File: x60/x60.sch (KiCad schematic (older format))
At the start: 150 parts, among them SW1 SW_Push, U1 ATmega32U4-AU, Y1 16mhz

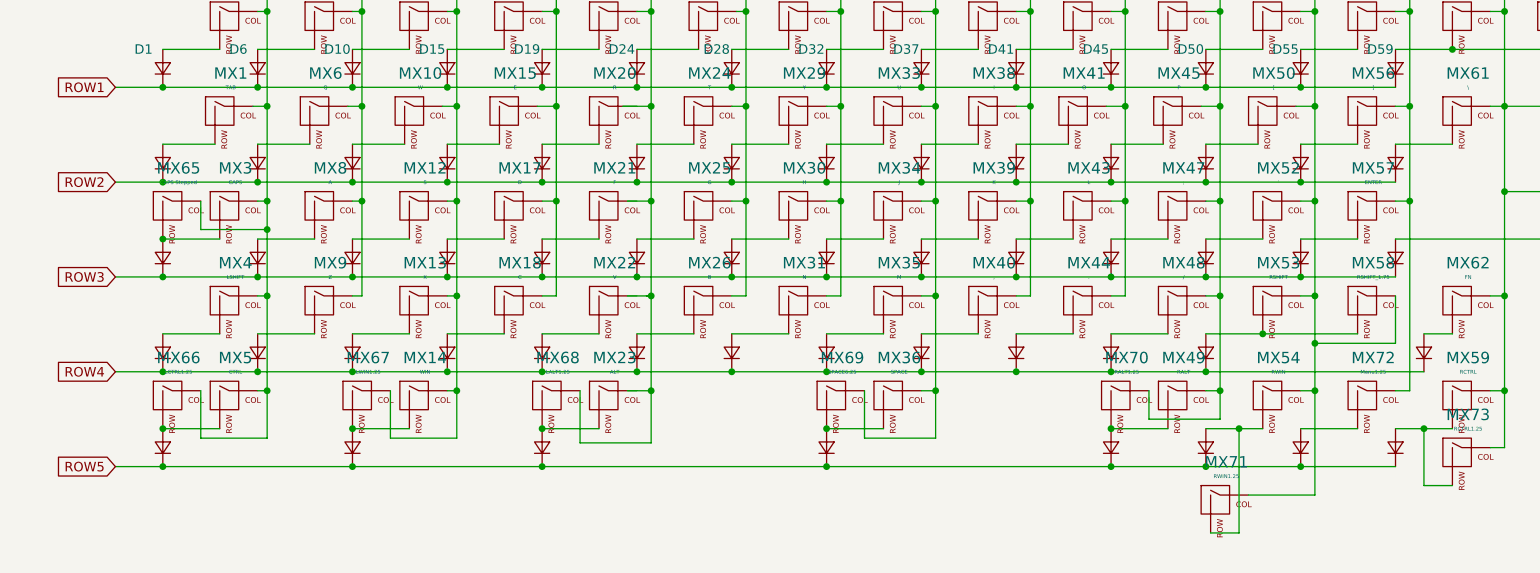
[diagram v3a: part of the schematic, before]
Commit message: aligned diodes
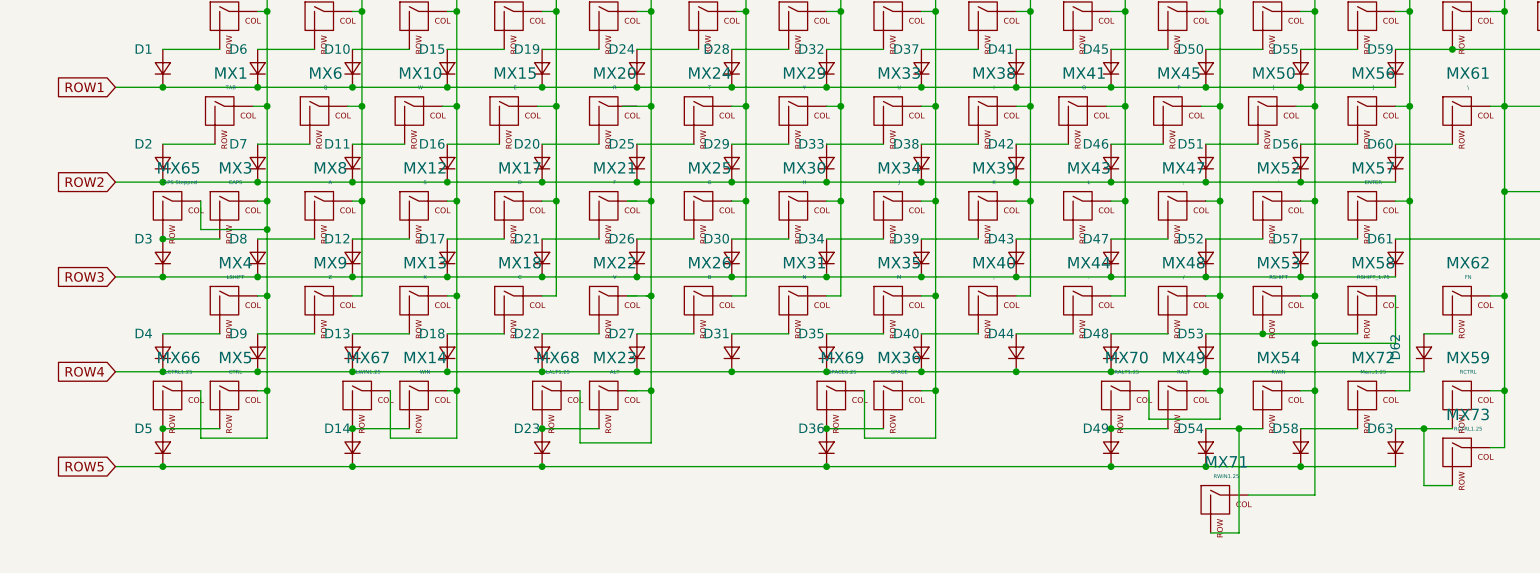
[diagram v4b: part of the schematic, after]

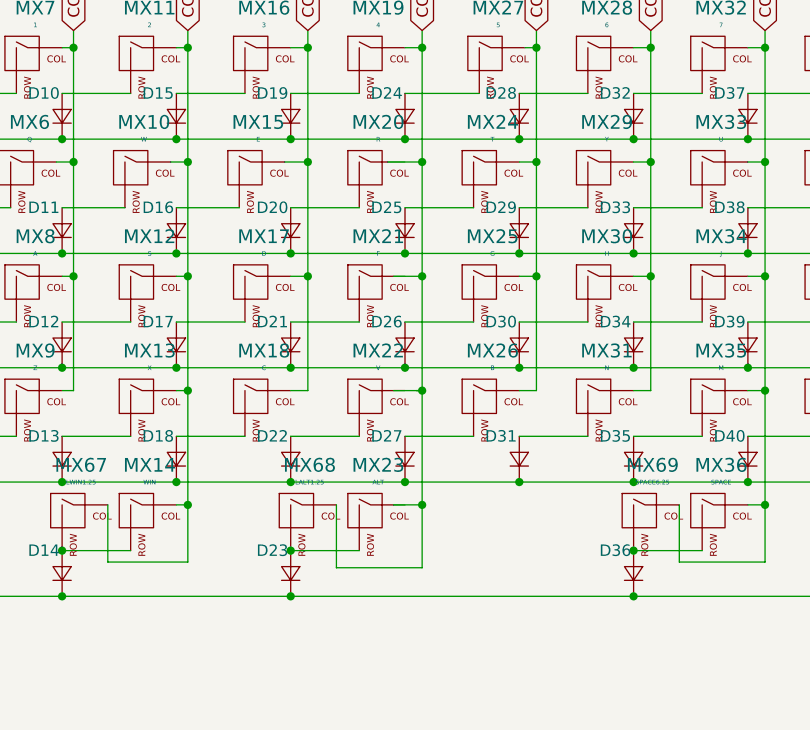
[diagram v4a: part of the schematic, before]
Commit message: fixed diode arrangement
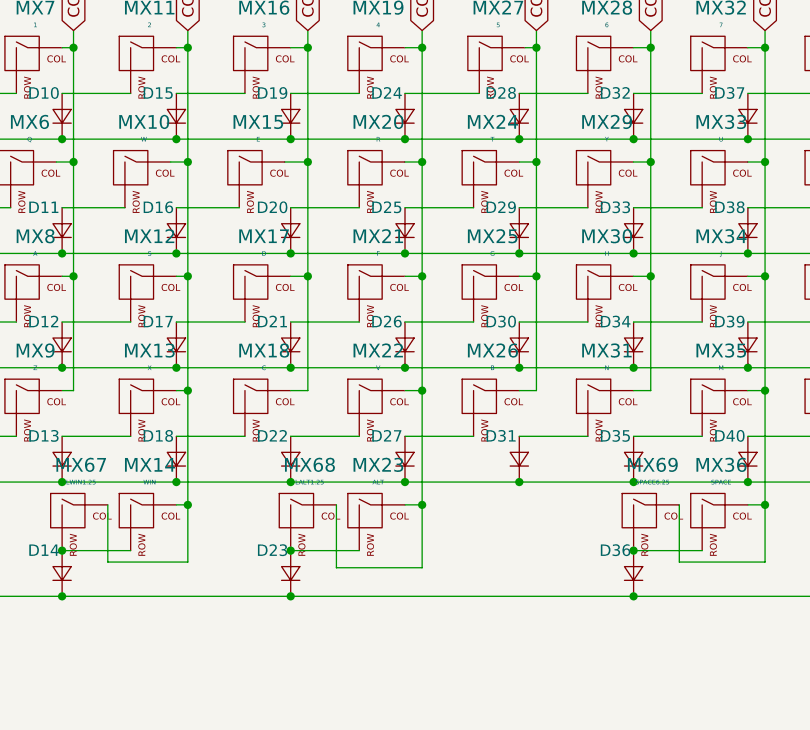
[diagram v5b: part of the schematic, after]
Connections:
- net COL5: now also MX20.1 (COL), MX21.1 (COL), MX22.1 (COL), MX23.1 (COL)

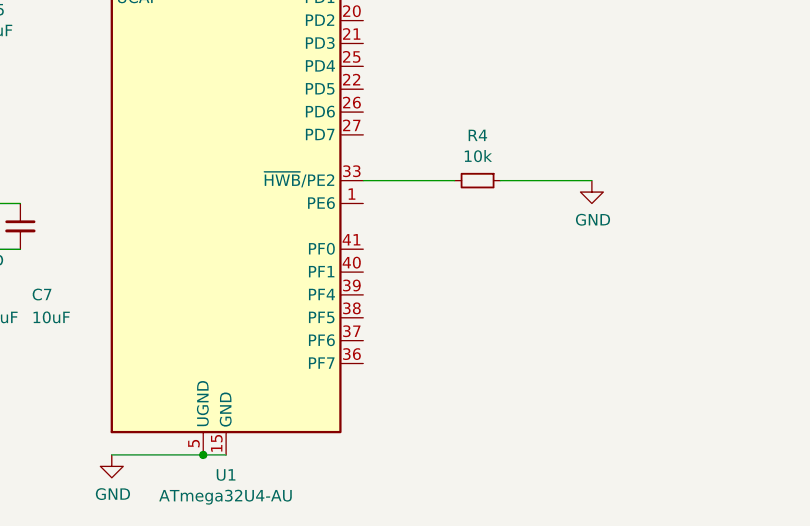
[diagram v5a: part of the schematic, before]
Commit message: connected rows to mcu
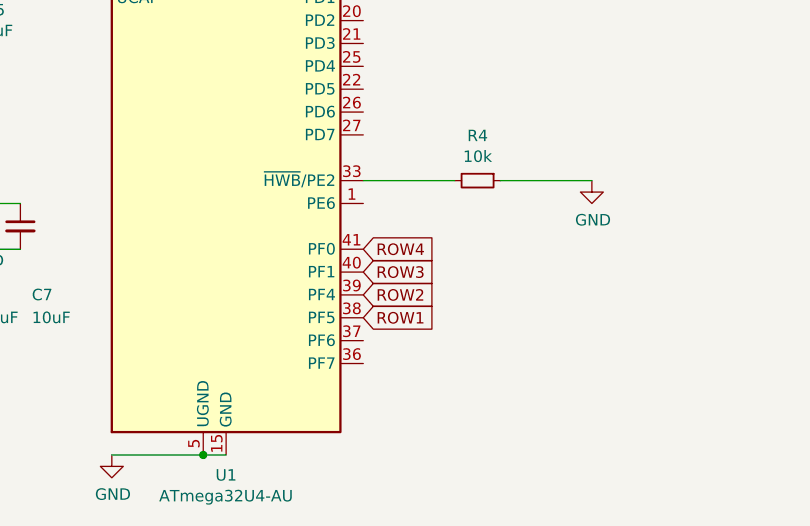
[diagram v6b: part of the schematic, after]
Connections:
- net ROW1: now also U1.38 (PF5)
- net ROW2: now also U1.39 (PF4)
- net ROW3: now also U1.40 (PF1)
- net ROW4: now also U1.41 (PF0)
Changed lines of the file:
@@
 Wire Wire Line
 	7325 1300 7325 1800
+Text GLabel 6075 7675 2    50   Input ~ 0
+ROW4
+Text GLabel 6075 7775 2    50   Input ~ 0
+ROW3
+Text GLabel 6075 7875 2    50   Input ~ 0
+ROW2
+Text GLabel 6075 7975 2    50   Input ~ 0
+ROW1
 $EndSCHEMATC

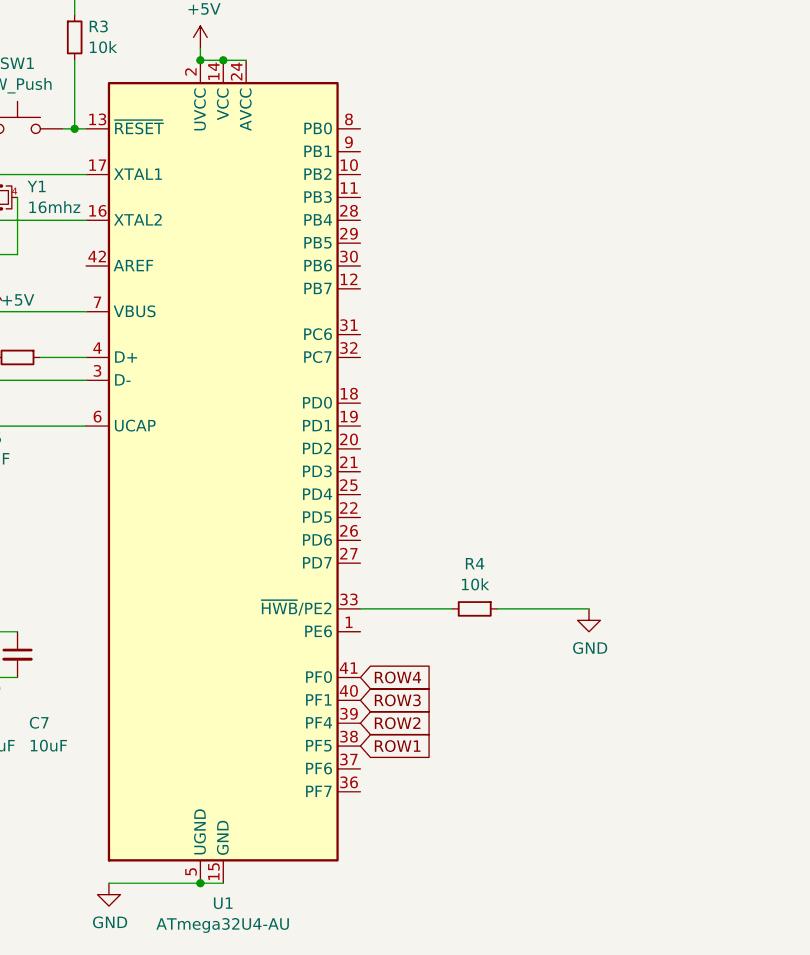
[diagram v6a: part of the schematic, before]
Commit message: wired all rows and columns to mcu
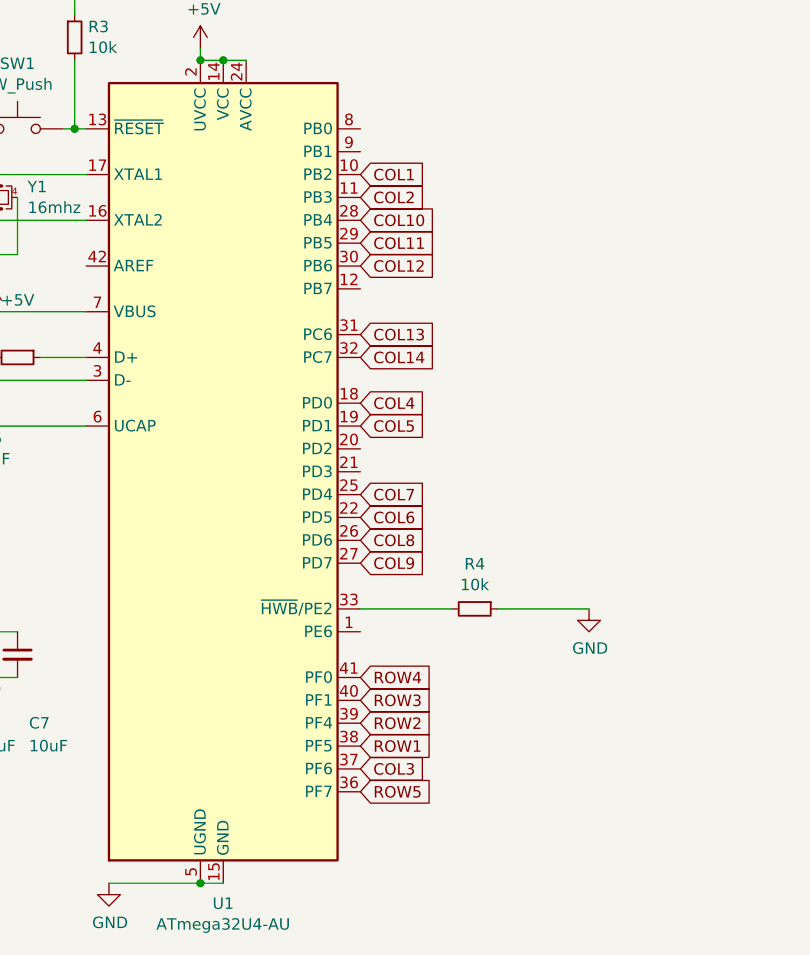
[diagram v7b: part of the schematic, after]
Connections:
- net COL1: now also U1.10 (PB2)
- net COL10: now also U1.28 (PB4)
- net COL11: now also U1.29 (PB5)
- net COL12: now also U1.30 (PB6)
- net COL13: now also U1.31 (PC6)
- net COL14: now also U1.32 (PC7)
- net COL2: now also U1.11 (PB3)
- net COL3: now also U1.37 (PF6)
- net COL4: now also U1.18 (PD0)
- net COL5: now also U1.19 (PD1)
- net COL6: now also U1.22 (PD5)
- net COL7: now also U1.25 (PD4)
- net COL8: now also U1.26 (PD6)
- net COL9: now also U1.27 (PD7)
- net ROW5: now also U1.36 (PF7)
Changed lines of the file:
@@
 Text GLabel 6075 7975 2    50   Input ~ 0
 ROW1
+Text GLabel 6075 8175 2    50   Input ~ 0
+ROW5
+Text GLabel 6075 5475 2    50   Input ~ 0
+COL1
+Text GLabel 6075 5575 2    50   Input ~ 0
+COL2
+Text GLabel 6075 8075 2    50   Input ~ 0
+COL3
+Text GLabel 6075 6475 2    50   Input ~ 0
+COL4
+Text GLabel 6075 6575 2    50   Input ~ 0
+COL5
+Text GLabel 6075 6975 2    50   Input ~ 0
+COL6
+Text GLabel 6075 6875 2    50   Input ~ 0
+COL7
+Text GLabel 6075 7075 2    50   Input ~ 0
+COL8
+Text GLabel 6075 7175 2    50   Input ~ 0
+COL9
+Text GLabel 6075 5675 2    50   Input ~ 0
+COL10
+Text GLabel 6075 5775 2    50   Input ~ 0
+COL11
+Text GLabel 6075 5875 2    50   Input ~ 0
+COL12
+Text GLabel 6075 6175 2    50   Input ~ 0
+COL13
+Text GLabel 6075 6275 2    50   Input ~ 0
+COL14
 $EndSCHEMATC

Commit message: flipped spacebar stabs
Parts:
- MX36: footprint MX_Only:MXOnly-7U-NoLED -> MX_Only:MXOnly-7U-ReversedStabilizers-NoLED
- MX69: footprint MX_Only:MXOnly-6.25U-NoLED -> MX_Only:MXOnly-6.25U-ReversedStabilizers-NoLED
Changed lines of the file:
@@
 F 0 "MX36" H 8633 3073 60  0000 C CNN
 F 1 "SPACE" H 8633 2999 20  0000 C CNN
-F 2 "MX_Only:MXOnly-7U-NoLED" H 7975 2825 60  0001 C CNN
+F 2 "MX_Only:MXOnly-7U-ReversedStabilizers-NoLED" H 7975 2825 60  0001 C CNN
 F 3 "" H 7975 2825 60  0001 C CNN
 	1    8600 2850
@@
 F 0 "MX69" H 8333 3073 60  0000 C CNN
 F 1 "SPACE6.25" H 8333 2999 20  0000 C CNN
-F 2 "MX_Only:MXOnly-6.25U-NoLED" H 7675 2825 60  0001 C CNN
+F 2 "MX_Only:MXOnly-6.25U-ReversedStabilizers-NoLED" H 7675 2825 60  0001 C CNN
 F 3 "" H 7675 2825 60  0001 C CNN
 	1    8300 2850
